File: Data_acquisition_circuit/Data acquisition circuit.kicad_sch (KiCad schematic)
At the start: 1 part, among them U2 STM32F767VGTx

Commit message: add max3232 file
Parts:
- added 8Mhz1: Crystal, symbol Device:Crystal
- added C1, C2: 20p-6030, symbol Device:C
- added C10, C11, C12, C13, C14, C5, C9: 104-6030, symbol Device:C
- added C15, C16, C17, C18, C19, C20: 10u-6030, symbol Device:C
- added C3, C4: 2.2u-1206, symbol Device:C
- added C6: 10n-6030, symbol Device:C
- added C7, C8: 1u-6030, symbol Device:C
- added PB1: 0.03R, symbol Device:R
- added R1, R2, R3: 10k-6030, symbol Device:R
- added R6, R7, R8, R9: 0, symbol Device:R
- renumbered U2 to U1
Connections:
- net GND: now reaches U1.10 (VSS), U1.26 (VSS), U1.49 (VSS), U1.74 (VSS), U1.99 (VSS)
- net GND: now also U1.19 (VSSA), C1.1, C10.1, C11.1, C12.1, C13.1, C14.1, C15.1, C16.1, C17.1, C18.1, C19.1, C2.1, C20.1, C3.1, C4.1, C5.1, C6.1, C7.1, C8.1, C9.1, R1.1, R2.1
- net +3.3V: now reaches U1.100 (VDD)
- net +3.3V: now also U1.11 (VDD), U1.27 (VDD), U1.50 (VDD), U1.6 (VBAT), U1.75 (VDD), C15.2, C16.2, C17.2, C18.2, C19.2, C20.2, C8.2, PB1.2, R3.1
- net at U1.12 (PH0): now also 8Mhz1.2, C1.2
- net at U1.13 (PH1): now also 8Mhz1.1, C2.2
- net NRST: now reaches U1.14 (NRST)
- net NRST: now also C5.2, R3.2
- net ADCx_IN10: now reaches U1.15 (PC0)
- net ADCx_IN11: now reaches U1.16 (PC1)
- net ADCx_IN12: now reaches U1.17 (PC2)
- net ADCx_IN13: now reaches U1.18 (PC3)
- net VREFMCU: now reaches U1.20 (VREF+)
- net at U1.21 (VDDA): now also C6.2, C7.2, PB1.1
- net ADCx_IN0: now reaches U1.22 (PA0)
- net ADCx_IN1: now reaches U1.23 (PA1)
- net ADCx_IN2: now reaches U1.24 (PA2)
- net ADCx_IN3: now reaches U1.25 (PA3)
- net AQ0: now reaches U1.28 (PA4)
- net AQ1: now reaches U1.29 (PA5)
- net ADCx_IN6: now reaches U1.30 (PA6)
- net ADCx_IN7: now reaches U1.31 (PA7)
- net ADCx_IN14: now reaches U1.32 (PC4)
- net ADCx_IN15: now reaches U1.33 (PC5)
- net ADCx_IN8: now reaches U1.34 (PB0)
- net ADCx_IN9: now reaches U1.35 (PB1)
- net BOOT1: now reaches U1.36 (PB2)
- net BOOT1: now also R1.2
- net at U1.48 (VCAP_1): now also C3.2
- net DQ0: now reaches U1.70 (PA11)
- net DQ1: now reaches U1.71 (PA12)
- net DBG_SWDIO: now reaches U1.72 (PA13)
- net at U1.73 (VCAP_2): now also C4.2
- net DBG_SWCLK: now reaches U1.76 (PA14)
- net at U1.78 (PC10): now also R6.1
- net at U1.79 (PC11): now also R7.1
- net Enc_A: now reaches U1.90 (PB4)
- net Enc_B: now reaches U1.91 (PB5)
- net DI0: now reaches U1.92 (PB6)
- net DI1: now reaches U1.93 (PB7)
- net at U1.94 (BOOT0): now also R2.2
- net at U1.95 (PB8): now also R8.1
- net at U1.96 (PB9): now also R9.1
- new net: C10.2, C11.2, C12.2, C13.2, C14.2, C9.2
- new net COM1_RX: R8.2
- new net COM1_TX: R9.2
- new net COM2_RX: R7.2
- new net COM2_TX: R6.2
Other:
- added sheet MAX3232 (untitled.kicad_sch)
- note added: "Data_acquisition_circuit"
- moved on the sheet: U1

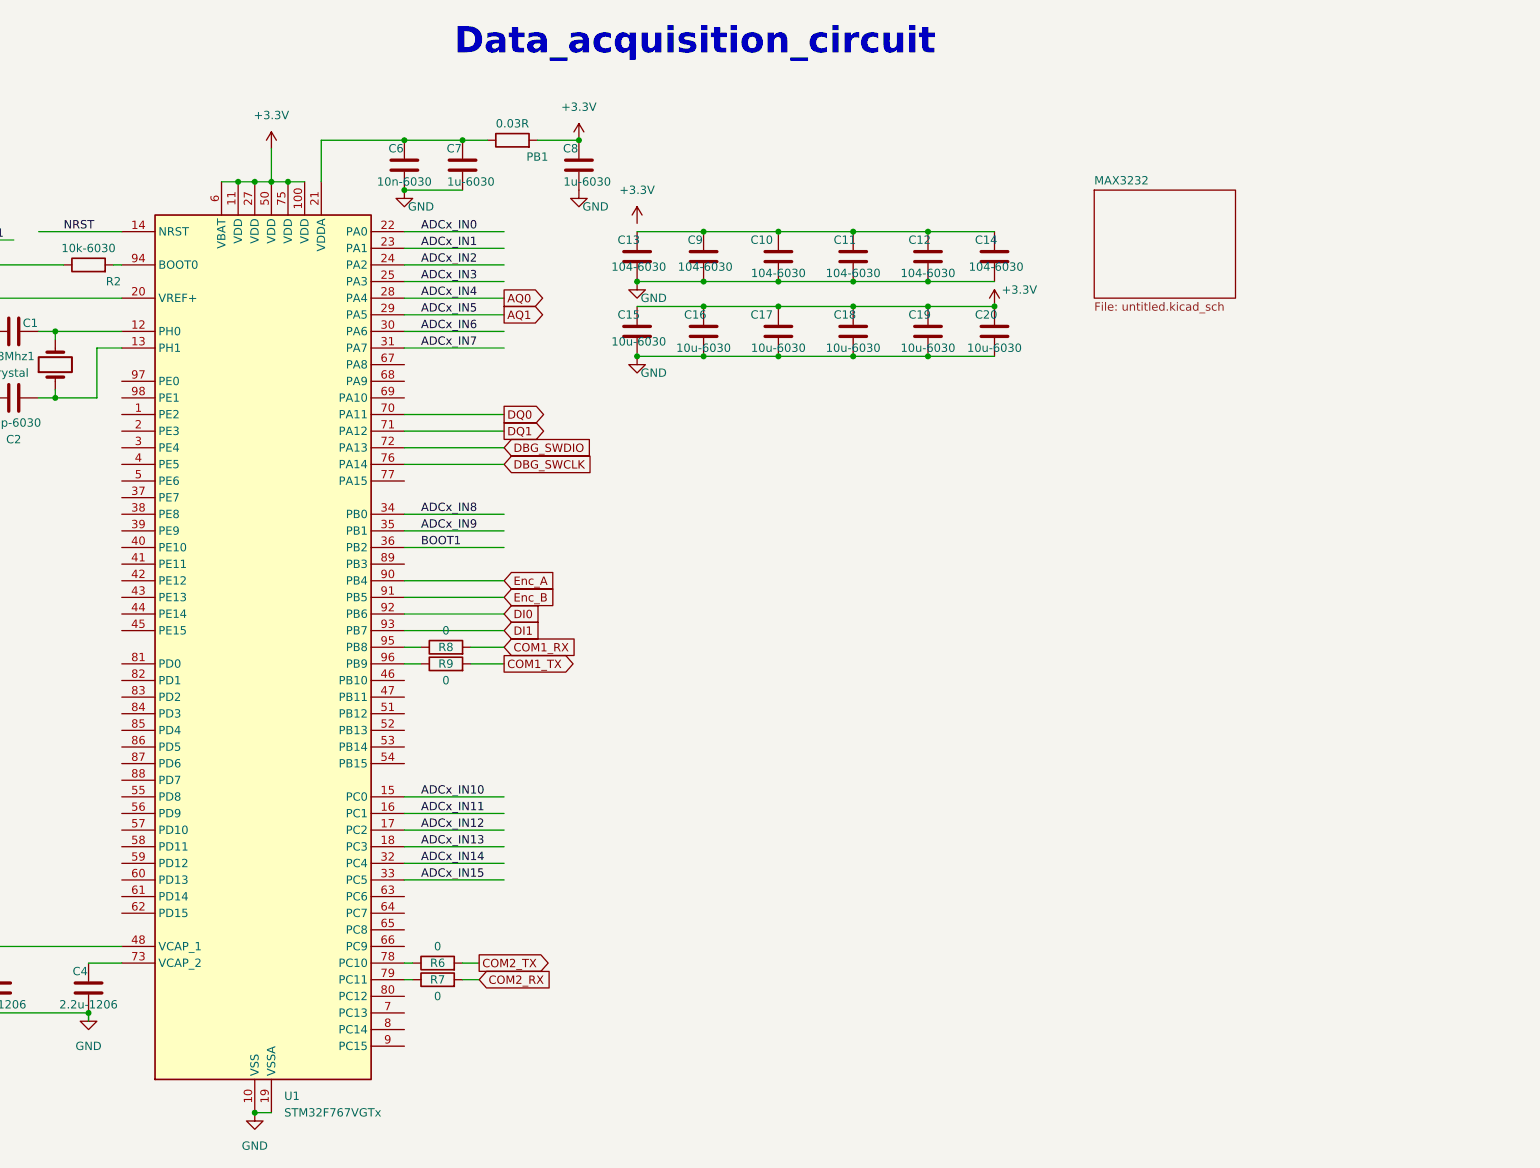
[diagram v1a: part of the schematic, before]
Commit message: add AQ, Encoder and digital input, power file
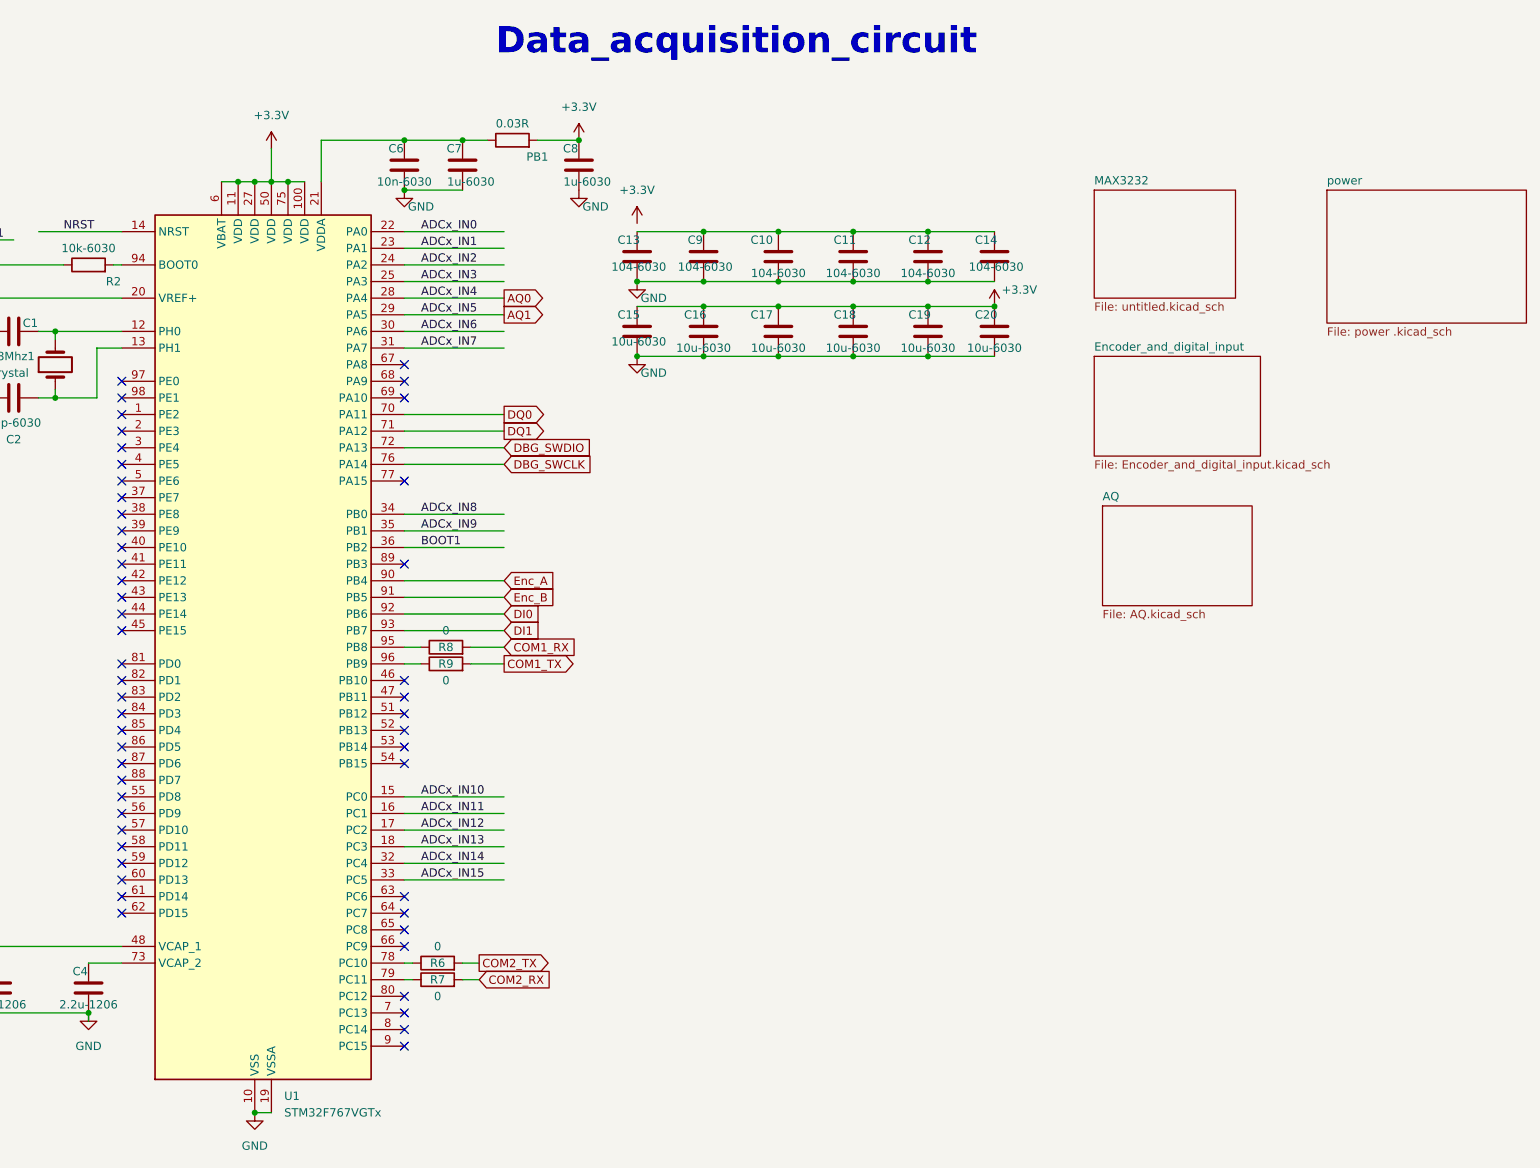
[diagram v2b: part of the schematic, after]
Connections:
- no-connect marks 0 -> 51
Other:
- added sheet AQ (AQ.kicad_sch)
- added sheet Encoder_and_digital_input (Encoder_and_digital_input.kicad_sch)
- added sheet power  (power .kicad_sch)
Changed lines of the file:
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@@
   (junction (at 80.01 44.45) (diameter 0) (color 0 0 0 0)
   )
+  (no_connect (at 59.69 123.19))
+  (no_connect (at 102.87 77.47))
+  (no_connect (at 59.69 133.35))
+  (no_connect (at 102.87 171.45))
+  (no_connect (at 102.87 72.39))
+  (no_connect (at 59.69 153.67))
+  (no_connect (at 59.69 80.01))
+  (no_connect (at 59.69 92.71))
+  (no_connect (at 59.69 151.13))
+  (no_connect (at 102.87 168.91))
+  (no_connect (at 102.87 161.29))
+  (no_connect (at 59.69 87.63))
+  (no_connect (at 59.69 143.51))
+  (no_connect (at 102.87 130.81))
+  (no_connect (at 59.69 110.49))
+  (no_connect (at 102.87 90.17))
+  (no_connect (at 59.69 118.11))
+  (no_connect (at 59.69 148.59))
+  (no_connect (at 102.87 176.53))
+  (no_connect (at 102.87 125.73))
+  (no_connect (at 59.69 74.93))
+  (no_connect (at 102.87 173.99))
+  (no_connect (at 59.69 146.05))
+  (no_connect (at 59.69 120.65))
+  (no_connect (at 59.69 138.43))
+  (no_connect (at 59.69 130.81))
+  (no_connect (at 59.69 97.79))
+  (no_connect (at 59.69 113.03))
+  (no_connect (at 102.87 128.27))
+  (no_connect (at 59.69 100.33))
+  (no_connect (at 59.69 140.97))
+  (no_connect (at 59.69 125.73))
+  (no_connect (at 59.69 77.47))
+  (no_connect (at 102.87 158.75))
+  (no_connect (at 59.69 107.95))
+  (no_connect (at 59.69 128.27))
+  (no_connect (at 102.87 123.19))
+  (no_connect (at 59.69 105.41))
+  (no_connect (at 59.69 85.09))
+  (no_connect (at 59.69 156.21))
+  (no_connect (at 102.87 102.87))
+  (no_connect (at 59.69 82.55))
+  (no_connect (at 102.87 74.93))
+  (no_connect (at 59.69 90.17))
+  (no_connect (at 102.87 120.65))
+  (no_connect (at 102.87 156.21))
+  (no_connect (at 59.69 135.89))
+  (no_connect (at 102.87 133.35))
+  (no_connect (at 102.87 153.67))
+  (no_connect (at 59.69 95.25))
+  (no_connect (at 59.69 102.87))
   (wire (pts (xy 80.01 186.69) (xy 82.55 186.69))
     (stroke (width 0) (type default))
@@
     (fill (type none))
   )
-  (text "Data_acquisition_circuit" (at 110.49 25.4 0)
+  (text "Data_acquisition_circuit" (at 116.84 25.4 0)
     (effects (font (size 4 4) (thickness 0.8) bold) (justify left bottom))
   )
@@
       )
     )
+  )
+  (sheet (at 243.84 45.72) (size 30.48 20.32) (fields_autoplaced)
+    (stroke (width 0.1524) (type solid))
+    (fill (color 0 0 0 0.0000))
+    (property "Sheetname" "power " (at 243.84 45.0084 0)
+      (effects (font (size 1.27 1.27)) (justify left bottom))
+    )
+    (property "Sheetfile" "power .kicad_sch" (at 243.84 66.6246 0)
+      (effects (font (size 1.27 1.27)) (justify left top))
+    )
+    (instances
+      (project "Data acquisition circuit"
+        (path "/1b7d87d8-ce09-4d95-b010-1b82030051eb" (page "5"))
+      )
+    )
+  )
+  (sheet (at 209.55 93.98) (size 22.86 15.24) (fields_autoplaced)
+    (stroke (width 0.1524) (type solid))
+    (fill (color 0 0 0 0.0000))
+    (property "Sheetname" "AQ" (at 209.55 93.2684 0)
+      (effects (font (size 1.27 1.27)) (justify left bottom))
+    )
+    (property "Sheetfile" "AQ.kicad_sch" (at 209.55 109.8046 0)
+      (effects (font (size 1.27 1.27)) (justify left top))
+    )
+    (instances
+      (project "Data acquisition circuit"
+        (path "/1b7d87d8-ce09-4d95-b010-1b82030051eb" (page "4"))
+      )
+    )
+  )
+  (sheet (at 208.28 71.12) (size 25.4 15.24) (fields_autoplaced)
+    (stroke (width 0.1524) (type solid))
+    (fill (color 0 0 0 0.0000))
+    (property "Sheetname" "Encoder_and_digital_input" (at 208.28 70.4084 0)
+      (effects (font (size 1.27 1.27)) (justify left bottom))
+    )
+    (property "Sheetfile" "Encoder_and_digital_input.kicad_sch" (at 208.28 86.9446 0)
+      (effects (font (size 1.27 1.27)) (justify left top))
+    )
+    (instances
+      (project "Data acquisition circuit"
+        (path "/1b7d87d8-ce09-4d95-b010-1b82030051eb" (page "3"))
+      )
+    )
